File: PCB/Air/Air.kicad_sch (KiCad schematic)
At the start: 15 parts, among them J1 Conn_01x02_Socket, M1 Fan, M2 Fan, M3 Fan, Q1 NMOS, Q2 NMOS, Q3 NMOS, U1 LM7805_TO220, U2 WRL-00691

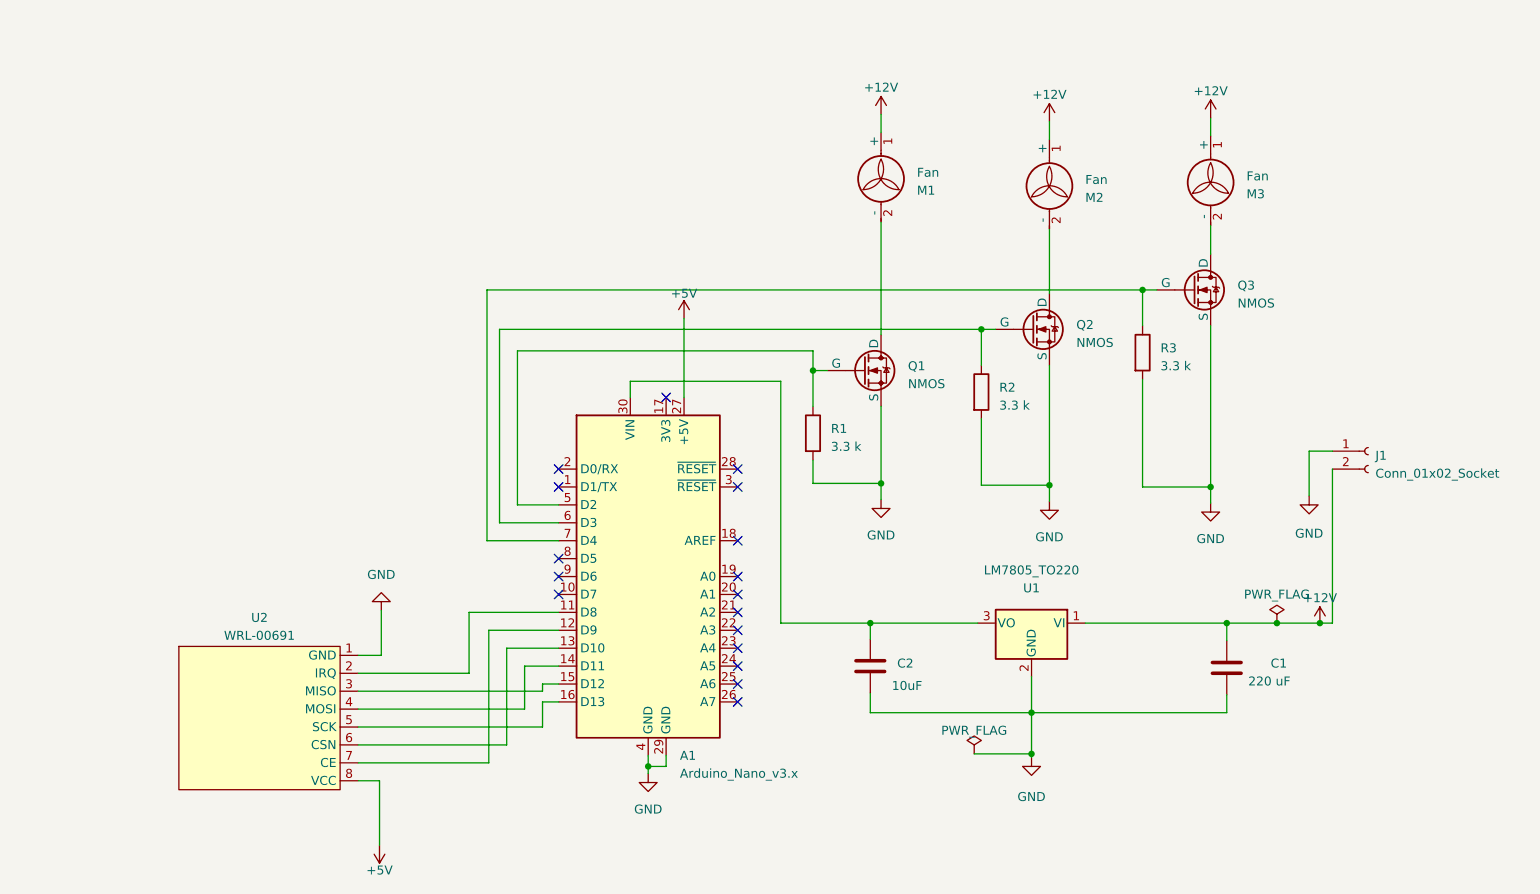
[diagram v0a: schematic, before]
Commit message: Updated PCB files; added desing files for caress and vibration
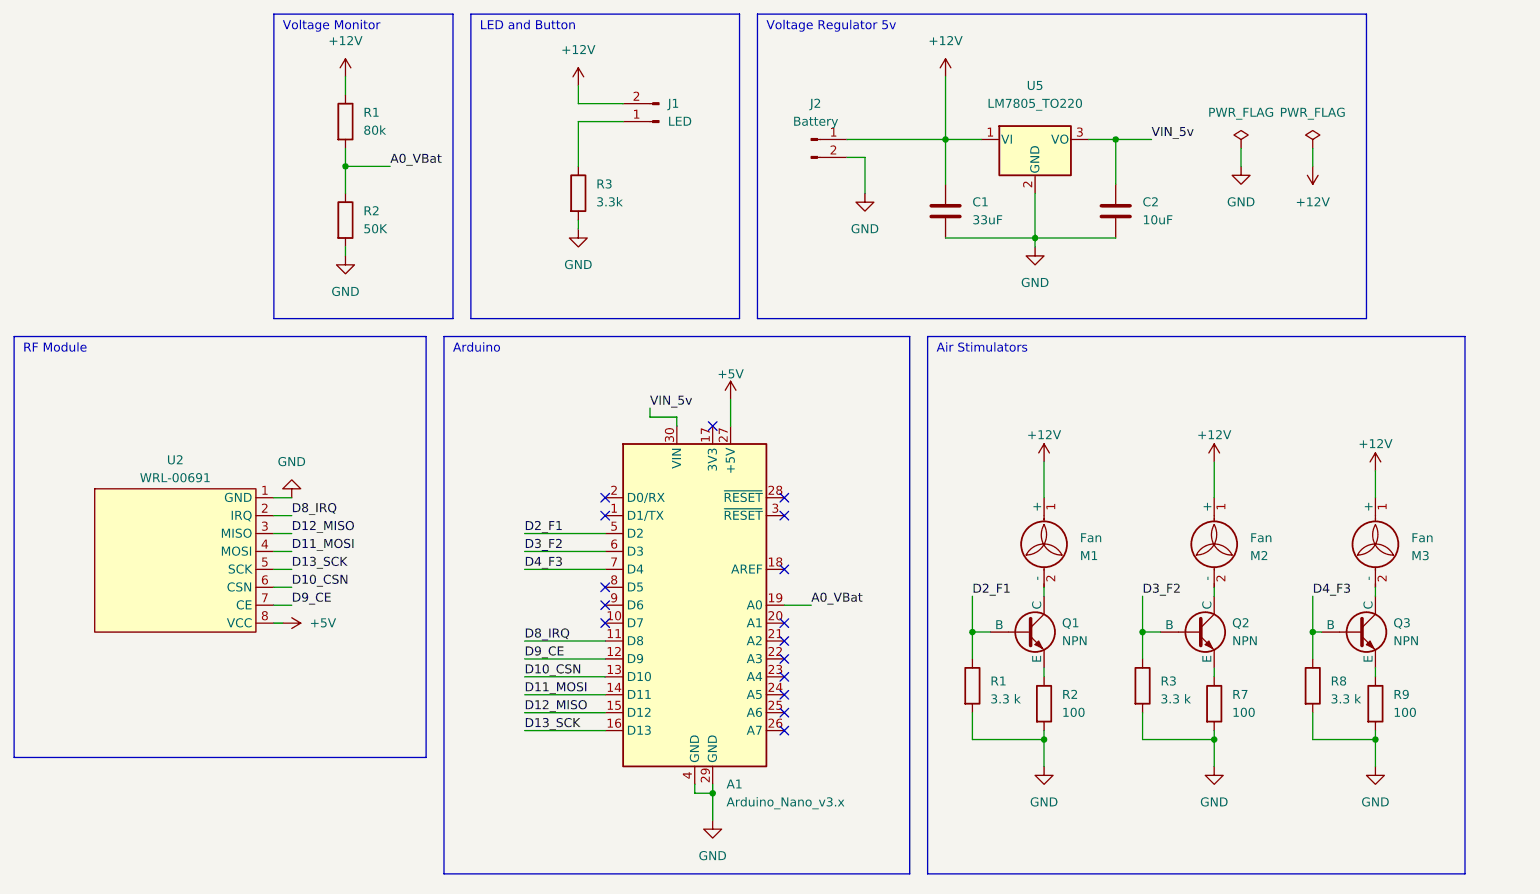
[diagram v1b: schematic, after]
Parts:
- removed J1: Conn_01x02_Socket, Connector_PinSocket_2.54mm:PinSocket_1x02_P2.54mm_Vertical, symbol Connector:Conn_01x02_Socket
- removed Q1, Q2, Q3: NMOS, Package_TO_SOT_THT:TO-220-3_Vertical, symbol Simulation_SPICE:NMOS
- removed R1, R2, R3: 3.3 k, Resistor_THT:R_Axial_DIN0207_L6.3mm_D2.5mm_P10.16mm_Horizontal, symbol Device:R
- removed U1: LM7805_TO220, Package_TO_SOT_THT:TO-220-3_Vertical, symbol Regulator_Linear:LM7805_TO220
- added J1: LED, Connector_JST:JST_EH_B2B-EH-A_1x02_P2.50mm_Vertical, symbol Connector:Conn_01x02_Pin
- added J2: Battery, Connector_JST:JST_EH_B2B-EH-A_1x02_P2.50mm_Vertical, symbol Connector:Conn_01x02_Pin
- added Q1, Q2, Q3: NPN, Connector_PinHeader_2.00mm:PinHeader_1x03_P2.00mm_Vertical, symbol Simulation_SPICE:NPN
- added R1, R3, R8: 3.3 k, Resistor_THT:R_Axial_DIN0207_L6.3mm_D2.5mm_P7.62mm_Horizontal, symbol Device:R
- added R1: 80k, Resistor_THT:R_Axial_DIN0207_L6.3mm_D2.5mm_P7.62mm_Horizontal, symbol Device:R
- added R2, R7, R9: 100, Resistor_THT:R_Axial_DIN0207_L6.3mm_D2.5mm_P7.62mm_Horizontal, symbol Device:R
- added R2: 50K, Resistor_THT:R_Axial_DIN0207_L6.3mm_D2.5mm_P7.62mm_Horizontal, symbol Device:R
- added R3: 3.3k, Resistor_THT:R_Axial_DIN0207_L6.3mm_D2.5mm_P7.62mm_Horizontal, symbol Device:R
- added U5: LM7805_TO220, Package_TO_SOT_THT:TO-220-3_Vertical, symbol Regulator_Linear:LM7805_TO220
- C1: value 220 uF -> 33uF; footprint Capacitor_THT:C_Radial_D6.3mm_H5.0mm_P2.50mm -> Capacitor_THT:C_Disc_D5.0mm_W2.5mm_P5.00mm
- C2: footprint Capacitor_THT:C_Radial_D6.3mm_H5.0mm_P2.50mm -> Capacitor_THT:C_Disc_D5.0mm_W2.5mm_P5.00mm
- U2: footprint Mod:WRL-00691 -> Mods:WRL-00691; symbol md:WRL-00691 -> MODS2:WRL-00691
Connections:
- net +12V: now also J1.2 (Pin_2), J2.1 (Pin_1), R1.1, U5.1 (VI)
- net GND: now also J2.2 (Pin_2), R1.2, R2.2, R2.2, R3.2, R3.2, R7.2, R8.2, R9.2, U5.2 (GND)
- net VIN_5v: now reaches A1.30 (VIN), C2.1
- net VIN_5v: now also U5.3 (VO)
- net D4_F3: now reaches A1.7 (D4)
- net D4_F3: now also Q3.2 (B), R8.1
- net D8_IRQ: now reaches A1.11 (D8), U2.2 (IRQ)
- net D12_MISO: now reaches A1.15 (D12), U2.3 (MISO)
- net D11_MOSI: now reaches A1.14 (D11), U2.4 (MOSI)
- net D13_SCK: now reaches A1.16 (D13), U2.5 (SCK)
- net D10_CSN: now reaches A1.13 (D10), U2.6 (CSN)
- net D9_CE: now reaches A1.12 (D9), U2.7 (CE)
- net A0_VBat: now reaches A1.19 (A0)
- net A0_VBat: now also R1.2, R2.1
- net D2_F1: now reaches A1.5 (D2)
- net D2_F1: now also Q1.2 (B), R1.1
- net D3_F2: now reaches A1.6 (D3)
- net D3_F2: now also Q2.2 (B), R3.1
- net at M1.2 (-): now also Q1.1 (C)
- net at M3.2 (-): now also Q3.1 (C)
- net at M2.2 (-): now also Q2.1 (C)
- new net: Q1.3 (E), R2.1
- new net: Q3.3 (E), R9.1
- new net: Q2.3 (E), R7.1
- new net: J1.1 (Pin_1), R3.1
- no-connect marks 17 -> 16
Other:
- note added: "Air Stimulators"
- note added: "Arduino"
- note added: "LED and Button"
- note added: "RF Module"
- note added: "Voltage Monitor"
- note added: "Voltage Regulator 5v"
- moved on the sheet: A1, U2
